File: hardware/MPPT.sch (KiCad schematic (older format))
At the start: 20 parts

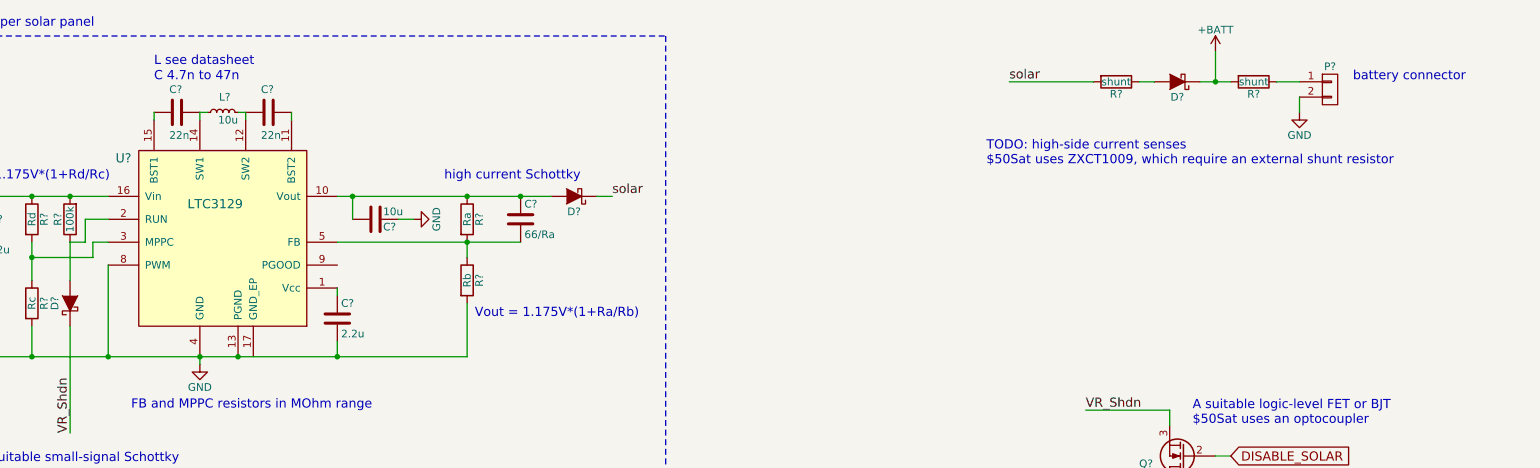
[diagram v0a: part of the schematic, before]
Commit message: Added ZXCT1009 current monitors
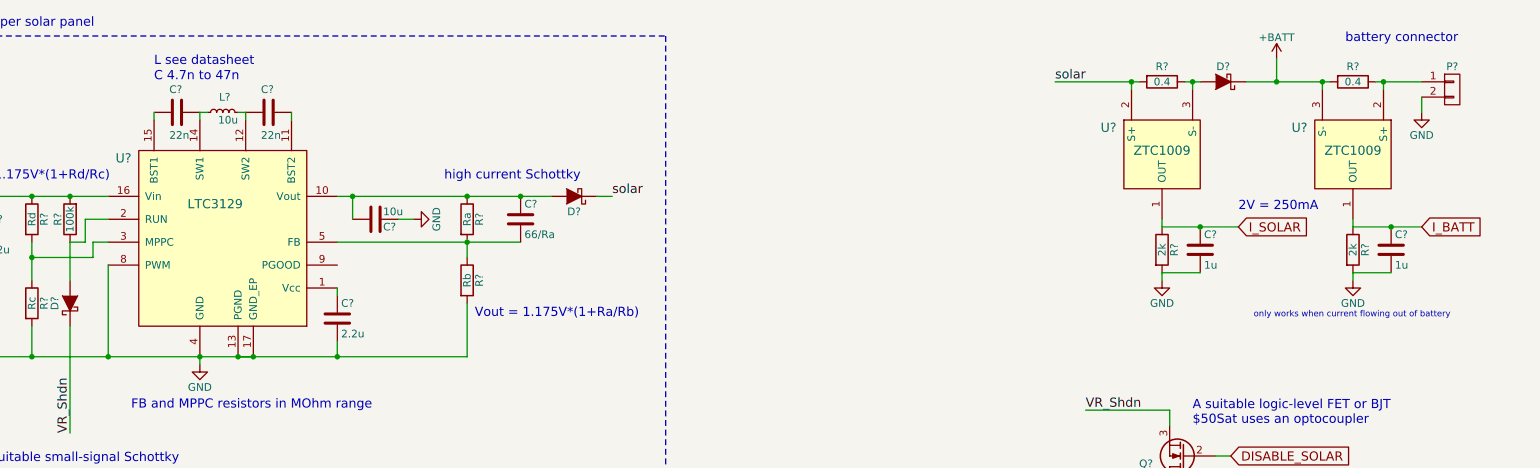
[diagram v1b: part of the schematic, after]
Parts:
- added C? (x2): 1u, symbol C
- added R? (x2): 2k, symbol R
- added U? (x2): ZTC1009, symbol ZTC1009
- R? (x2): value shunt -> 0.4
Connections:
- net +BATT: now also U?.3 (S-)
- net GND: now also U?.17 (GND_EP), C?.2, C?.2, R?.2, R?.2
- net solar: now also U?.2 (S+)
- net at D?.2 (A), R?.1: now also U?.3 (S-)
- net at P?.1 (P1), R?.1: now also U?.2 (S+)
- new net I_BATT: C?.1, R?.1, U?.1 (OUT)
- new net I_SOLAR: C?.1, R?.1, U?.1 (OUT)
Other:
- note added: "2V = 250mA"
- note added: "only works when current flowing out of battery"
- note removed: "TODO: high-side current senses\n$50Sat uses ZXCT1009, which require an external shunt resistor"
- moved on the sheet: D?, P?, R?
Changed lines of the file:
@@
 EESchema Schematic File Version 2
+LIBS:easat2-rescue
 LIBS:power
 LIBS:device
@@
 Sheet 2 2
 Title "EASAT-2 MPPT"
-Date "2016-08-26"
+Date "2016-08-27"
 Rev ""
 Comp "AMSAT-EA"
@@
 C 4.7n to 47n
 Wire Wire Line
-	2250 2250 2250 2850
+	2250 2850 2250 2250
 Connection ~ 2250 2850
 Text GLabel 1150 1800 0    60   Input ~ 0
@@
 L R R?
 U 1 1 57C0BCA9
-P 8850 1050
-F 0 "R?" V 8930 1050 50  0000 C CNN
-F 1 "shunt" V 8850 1050 50  0000 C CNN
-F 2 "" V 8780 1050 30  0000 C CNN
-F 3 "" H 8850 1050 30  0000 C CNN
-	1    8850 1050
+P 9150 1050
+F 0 "R?" V 9050 1050 50  0000 C CNN
+F 1 "0.4" V 9150 1050 50  0000 C CNN
+F 2 "" V 9080 1050 30  0000 C CNN
+F 3 "" H 9150 1050 30  0000 C CNN
+	1    9150 1050
 	0    1    1    0
 $EndComp
@@
 L R R?
 U 1 1 57C0BCEE
-P 9750 1050
-F 0 "R?" V 9830 1050 50  0000 C CNN
-F 1 "shunt" V 9750 1050 50  0000 C CNN
-F 2 "" V 9680 1050 30  0000 C CNN
-F 3 "" H 9750 1050 30  0000 C CNN
-	1    9750 1050
+P 10400 1050
+F 0 "R?" V 10300 1050 50  0000 C CNN
+F 1 "0.4" V 10400 1050 50  0000 C CNN
+F 2 "" V 10330 1050 30  0000 C CNN
+F 3 "" H 10400 1050 30  0000 C CNN
+	1    10400 1050
 	0    1    1    0
 $EndComp
@@
 $EndComp
 Wire Wire Line
-	5150 1800 3750 1800
+	3750 1800 5150 1800
 Text Notes 4450 1700 0    60   ~ 0
 high current Schottky
@@
 	5450 1800 5550 1800
 Wire Wire Line
-	8700 1050 8150 1050
-Text Label 8150 1050 0    60   ~ 0
+	9000 1050 8450 1050
+Text Label 8450 1050 0    60   ~ 0
 solar
-Text Notes 8000 1600 0    60   ~ 0
-TODO: high-side current senses\n$50Sat uses ZXCT1009, which require an external shunt resistor
 $Comp
 L D_Schottky D?
 U 1 1 57C0D536
-P 9250 1050
-F 0 "D?" H 9250 1150 50  0000 C CNN
-F 1 "D_Schottky" H 9250 950 50  0001 C CNN
-F 2 "" H 9250 1050 60  0000 C CNN
-F 3 "" H 9250 1050 60  0000 C CNN
-	1    9250 1050
+P 9550 1050
+F 0 "D?" H 9550 950 50  0000 C CNN
+F 1 "D_Schottky" H 9550 950 50  0001 C CNN
+F 2 "" H 9550 1050 60  0000 C CNN
+F 3 "" H 9550 1050 60  0000 C CNN
+	1    9550 1050
 	-1   0    0    1
 $EndComp
 Wire Wire Line
-	9000 1050 9100 1050
-Wire Wire Line
-	9400 1050 9600 1050
-Wire Wire Line
-	9500 1050 9500 850
-Connection ~ 9500 1050
+	9300 1050 9400 1050
 $Comp
 L +BATT #PWR?
 U 1 1 57C0D8F3
-P 9500 850
-F 0 "#PWR?" H 9500 700 50  0001 C CNN
-F 1 "+BATT" H 9500 990 50  0000 C CNN
-F 2 "" H 9500 850 60  0000 C CNN
-F 3 "" H 9500 850 60  0000 C CNN
-	1    9500 850
+P 9900 900
+F 0 "#PWR?" H 9900 750 50  0001 C CNN
+F 1 "+BATT" H 9900 1040 50  0000 C CNN
+F 2 "" H 9900 900 60  0000 C CNN
+F 3 "" H 9900 900 60  0000 C CNN
+	1    9900 900
 	1    0    0    -1
 $EndComp
@@
 L CONN_01X02 P?
 U 1 1 57C0DB54
-P 10250 1100
-F 0 "P?" H 10250 1250 50  0000 C CNN
-F 1 "CONN_01X02" V 10350 1100 50  0001 C CNN
-F 2 "" H 10250 1100 60  0000 C CNN
-F 3 "" H 10250 1100 60  0000 C CNN
-	1    10250 1100
-	1    0    0    -1
-$EndComp
-Wire Wire Line
-	9900 1050 10050 1050
+P 11050 1100
+F 0 "P?" H 11050 1250 50  0000 C CNN
+F 1 "CONN_01X02" V 11150 1100 50  0001 C CNN
+F 2 "" H 11050 1100 60  0000 C CNN
+F 3 "" H 11050 1100 60  0000 C CNN
+	1    11050 1100
+	1    0    0    -1
+$EndComp
 $Comp
 L GND #PWR?
 U 1 1 57C0DBDE
-P 10050 1250
-F 0 "#PWR?" H 10050 1000 50  0001 C CNN
-F 1 "GND" H 10050 1100 50  0000 C CNN
-F 2 "" H 10050 1250 60  0000 C CNN
-F 3 "" H 10050 1250 60  0000 C CNN
-	1    10050 1250
-	1    0    0    -1
-$EndComp
-Wire Wire Line
-	10050 1150 10050 1250
-Text Notes 10400 1050 0    60   ~ 0
+P 10850 1250
+F 0 "#PWR?" H 10850 1000 50  0001 C CNN
+F 1 "GND" H 10850 1100 50  0000 C CNN
+F 2 "" H 10850 1250 60  0000 C CNN
+F 3 "" H 10850 1250 60  0000 C CNN
+	1    10850 1250
+	1    0    0    -1
+$EndComp
+Text Notes 10350 800  0    60   ~ 0
 battery connector
 Wire Notes Line
@@
 Wire Notes Line
 	700  3600 700  750
+Wire Wire Line
+	3100 2850 3200 2850
+Connection ~ 3200 2850
+Wire Wire Line
+	10850 1150 10850 1250
+Wire Wire Line
+	10550 1050 10850 1050
+Wire Wire Line
+	10600 1100 10600 1050
+Connection ~ 10600 1050
+Wire Wire Line
+	9900 900  9900 1050
+Wire Wire Line
+	9700 1050 10250 1050
+Wire Wire Line
+	10200 1100 10200 1050
+Connection ~ 10200 1050
+Connection ~ 9900 1050
+Wire Wire Line
+	8950 1100 8950 1050
+Connection ~ 8950 1050
+Wire Wire Line
+	9350 1100 9350 1050
+Connection ~ 9350 1050
+$Comp
+L R R?
+U 1 1 57C1C3E9
+P 9150 2150
+F 0 "R?" V 9230 2150 50  0000 C CNN
+F 1 "2k" V 9150 2150 50  0000 C CNN
+F 2 "" V 9080 2150 30  0000 C CNN
+F 3 "" H 9150 2150 30  0000 C CNN
+	1    9150 2150
+	1    0    0    -1
+$EndComp
+$Comp
+L R R?
+U 1 1 57C1C434
+P 10400 2150
+F 0 "R?" V 10480 2150 50  0000 C CNN
+F 1 "2k" V 10400 2150 50  0000 C CNN
+F 2 "" V 10330 2150 30  0000 C CNN
+F 3 "" H 10400 2150 30  0000 C CNN
+	1    10400 2150
+	1    0    0    -1
+$EndComp
+Wire Wire Line
+	9150 1950 9150 2000
+Wire Wire Line
+	10400 1950 10400 2000
+$Comp
+L ZTC1009 U?
+U 1 1 57C1C31D
+P 9150 1500
+F 0 "U?" H 8800 1650 60  0000 C CNN
+F 1 "ZTC1009" H 9150 1500 60  0000 C CNN
+F 2 "" H 9150 1500 60  0000 C CNN
+F 3 "" H 9150 1500 60  0000 C CNN
+	1    9150 1500
+	1    0    0    -1
+$EndComp
+$Comp
+L ZTC1009 U?
+U 1 1 57C1C370
+P 10400 1500
+F 0 "U?" H 10750 1650 60  0000 C CNN
+F 1 "ZTC1009" H 10400 1500 60  0000 C CNN
+F 2 "" H 10400 1500 60  0000 C CNN
+F 3 "" H 10400 1500 60  0000 C CNN
+	1    10400 1500
+	-1   0    0    -1
+$EndComp
+$Comp
+L GND #PWR?
+U 1 1 57C1C479
+P 9150 2350
+F 0 "#PWR?" H 9150 2100 50  0001 C CNN
+F 1 "GND" H 9150 2200 50  0000 C CNN
+F 2 "" H 9150 2350 60  0000 C CNN
+F 3 "" H 9150 2350 60  0000 C CNN
+	1    9150 2350
+	1    0    0    -1
+$EndComp
+$Comp
+L GND #PWR?
+U 1 1 57C1C4BD
+P 10400 2350
+F 0 "#PWR?" H 10400 2100 50  0001 C CNN
+F 1 "GND" H 10400 2200 50  0000 C CNN
+F 2 "" H 10400 2350 60  0000 C CNN
+F 3 "" H 10400 2350 60  0000 C CNN
+	1    10400 2350
+	1    0    0    -1
+$EndComp
+Wire Wire Line
+	9150 2300 9150 2350
+Wire Wire Line
+	10400 2300 10400 2350
+$Comp
+L C C?
+U 1 1 57C1C65F
+P 9400 2150
+F 0 "C?" H 9425 2250 50  0000 L CNN
+F 1 "1u" H 9425 2050 50  0000 L CNN
+F 2 "" H 9438 2000 30  0000 C CNN
+F 3 "" H 9400 2150 60  0000 C CNN
+	1    9400 2150
+	1    0    0    -1
+$EndComp
+Wire Wire Line
+	9150 2300 9400 2300
+Wire Wire Line
+	9150 2000 9650 2000
+$Comp
+L C C?
+U 1 1 57C1C78D
+P 10650 2150
+F 0 "C?" H 10675 2250 50  0000 L CNN
+F 1 "1u" H 10675 2050 50  0000 L CNN
+F 2 "" H 10688 2000 30  0000 C CNN
+F 3 "" H 10650 2150 60  0000 C CNN
+	1    10650 2150
+	1    0    0    -1
+$EndComp
+Wire Wire Line
+	10400 2000 10850 2000
+Wire Wire Line
+	10650 2300 10400 2300
+Connection ~ 9400 2000
+Connection ~ 10650 2000
+Text GLabel 9650 2000 2    60   Input ~ 0
+I_SOLAR
+Text GLabel 10850 2000 2    60   Input ~ 0
+I_BATT
+Text Notes 9750 2600 0    40   ~ 0
+only works when current flowing out of battery
+Text Notes 9650 1900 0    60   ~ 0
+2V = 250mA
 $EndSCHEMATC

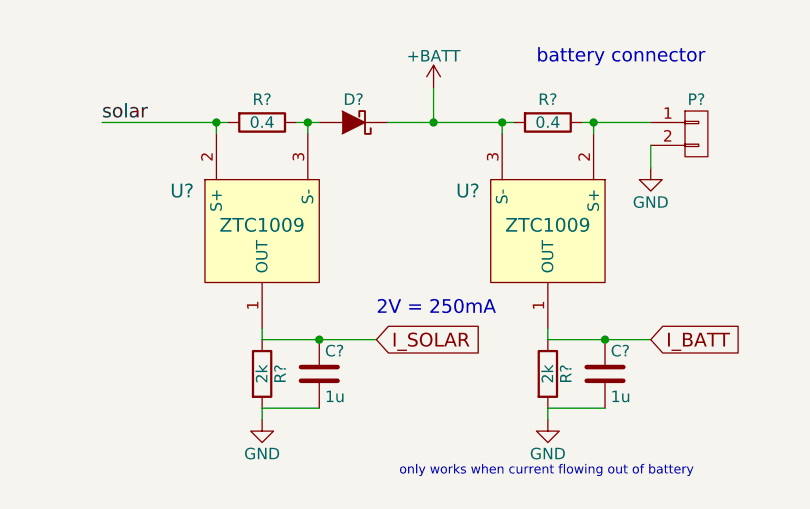
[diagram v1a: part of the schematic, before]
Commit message: Corrected current shunt name: ZXCT1009
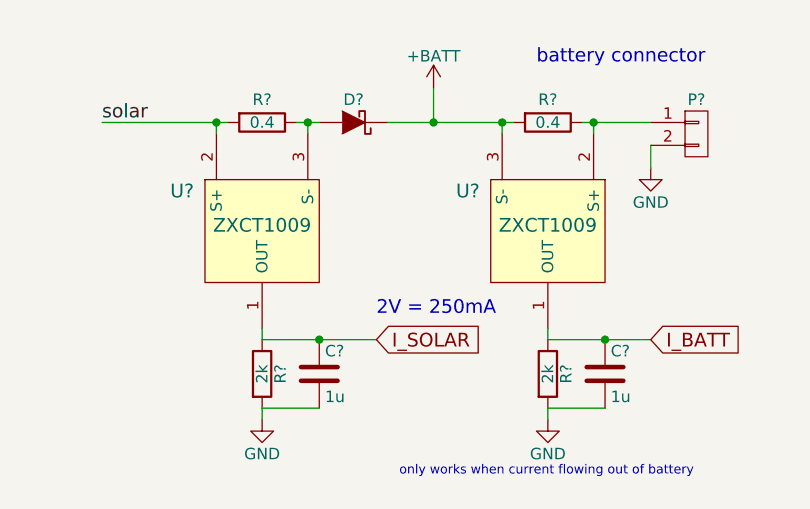
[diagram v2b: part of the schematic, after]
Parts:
- removed U? (x2): ZTC1009, symbol ZTC1009
- added U? (x2): ZXCT1009, symbol ZXCT1009
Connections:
- net +BATT: now also U?.3 (S-)
- net I_BATT: now also U?.1 (OUT)
- net I_SOLAR: now also U?.1 (OUT)
- net solar: now also U?.2 (S+)
- net at D?.2 (A), R?.1: now also U?.3 (S-)
- net at P?.1 (P1), R?.1: now also U?.2 (S+)
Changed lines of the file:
@@
 Sheet 2 2
 Title "EASAT-2 MPPT"
-Date "2016-08-27"
+Date "2016-09-06"
 Rev ""
 Comp "AMSAT-EA"
@@
 Wire Wire Line
 	10400 1950 10400 2000
-$Comp
-L ZTC1009 U?
-U 1 1 57C1C31D
-P 9150 1500
-F 0 "U?" H 8800 1650 60  0000 C CNN
-F 1 "ZTC1009" H 9150 1500 60  0000 C CNN
-F 2 "" H 9150 1500 60  0000 C CNN
-F 3 "" H 9150 1500 60  0000 C CNN
-	1    9150 1500
-	1    0    0    -1
-$EndComp
-$Comp
-L ZTC1009 U?
-U 1 1 57C1C370
-P 10400 1500
-F 0 "U?" H 10750 1650 60  0000 C CNN
-F 1 "ZTC1009" H 10400 1500 60  0000 C CNN
-F 2 "" H 10400 1500 60  0000 C CNN
-F 3 "" H 10400 1500 60  0000 C CNN
-	1    10400 1500
-	-1   0    0    -1
-$EndComp
 $Comp
 L GND #PWR?
@@
 Text Notes 9650 1900 0    60   ~ 0
 2V = 250mA
+$Comp
+L ZXCT1009 U?
+U 1 1 57CE8C1C
+P 9150 1500
+F 0 "U?" H 8800 1650 60  0000 C CNN
+F 1 "ZXCT1009" H 9150 1500 60  0000 C CNN
+F 2 "" H 9150 1500 60  0000 C CNN
+F 3 "" H 9150 1500 60  0000 C CNN
+	1    9150 1500
+	1    0    0    -1
+$EndComp
+$Comp
+L ZXCT1009 U?
+U 1 1 57CE8D8E
+P 10400 1500
+F 0 "U?" H 10750 1650 60  0000 C CNN
+F 1 "ZXCT1009" H 10400 1500 60  0000 C CNN
+F 2 "" H 10400 1500 60  0000 C CNN
+F 3 "" H 10400 1500 60  0000 C CNN
+	1    10400 1500
+	-1   0    0    -1
+$EndComp
 $EndSCHEMATC
